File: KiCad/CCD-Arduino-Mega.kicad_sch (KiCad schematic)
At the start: 36 parts, among them J1 CCD+, J10 +5V, J11 PWM, J12 PWM, J13 COMMUNICATION, J2 CCD-, J3 Ground, J4 CCD-BUS, J5 Button, J6 POWER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

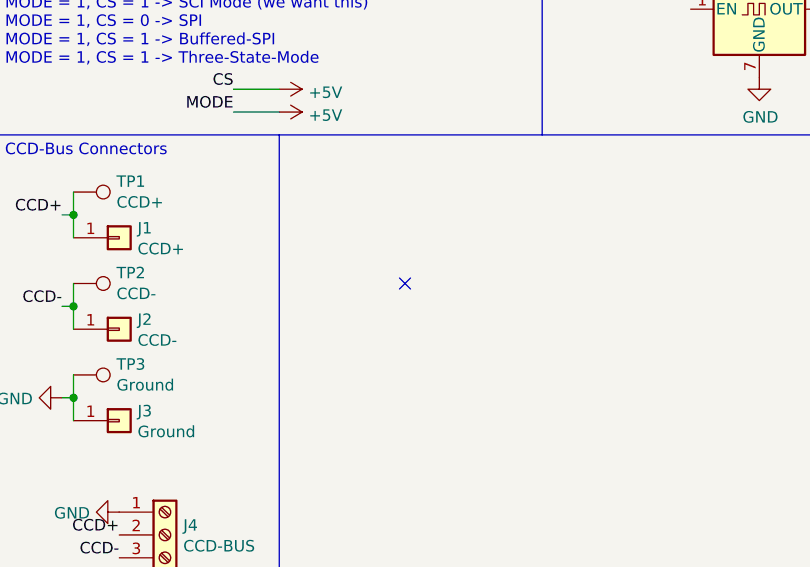
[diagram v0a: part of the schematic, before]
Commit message: implement ZIF-Socket
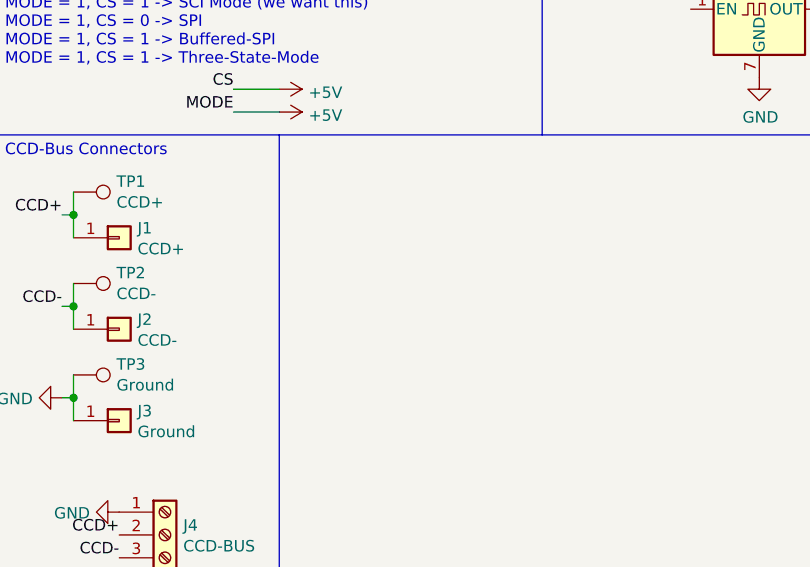
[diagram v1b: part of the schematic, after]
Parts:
- U1: footprint Package_DIP:DIP-14_W7.62mm -> Socket:DIP_Socket-14_W4.3_W5.08_W7.62_W10.16_W10.9_3M_214-3339-00-0602J
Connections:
- no-connect marks 6 -> 5
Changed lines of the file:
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@@
   (no_connect (at 76.2 49.53))
   (no_connect (at 76.2 22.86))
-  (no_connect (at 58.42 137.16))
   (polyline (pts (xy 12.7 170.18) (xy 44.45 170.18))
     (stroke (width 0) (type default) (color 0 0 0 0))
@@
     (property "Reference" "U1" (id 0) (at 41.91 18.6182 0))
     (property "Value" "Conn_02x07_Counter_Clockwise" (id 1) (at 41.91 20.9296 0))
-    (property "Footprint" "Package_DIP:DIP-14_W7.62mm" (id 2) (at 40.64 31.75 0)
+    (property "Footprint" "Socket:DIP_Socket-14_W4.3_W5.08_W7.62_W10.16_W10.9_3M_214-3339-00-0602J" (id 2) (at 40.64 31.75 0)
       (effects (font (size 1.27 1.27)) hide)
     )
@@
     )
     (path "/23352efa-710c-4ca4-98a5-fd92267e586c"
-      (reference "U1") (unit 1) (value "Conn_02x07_Counter_Clockwise") (footprint "Package_DIP:DIP-14_W7.62mm")
+      (reference "U1") (unit 1) (value "Conn_02x07_Counter_Clockwise") (footprint "Socket:DIP_Socket-14_W4.3_W5.08_W7.62_W10.16_W10.9_3M_214-3339-00-0602J")
     )
     (path "/99ad6875-75cb-427f-92c4-5fd2633b46f0"

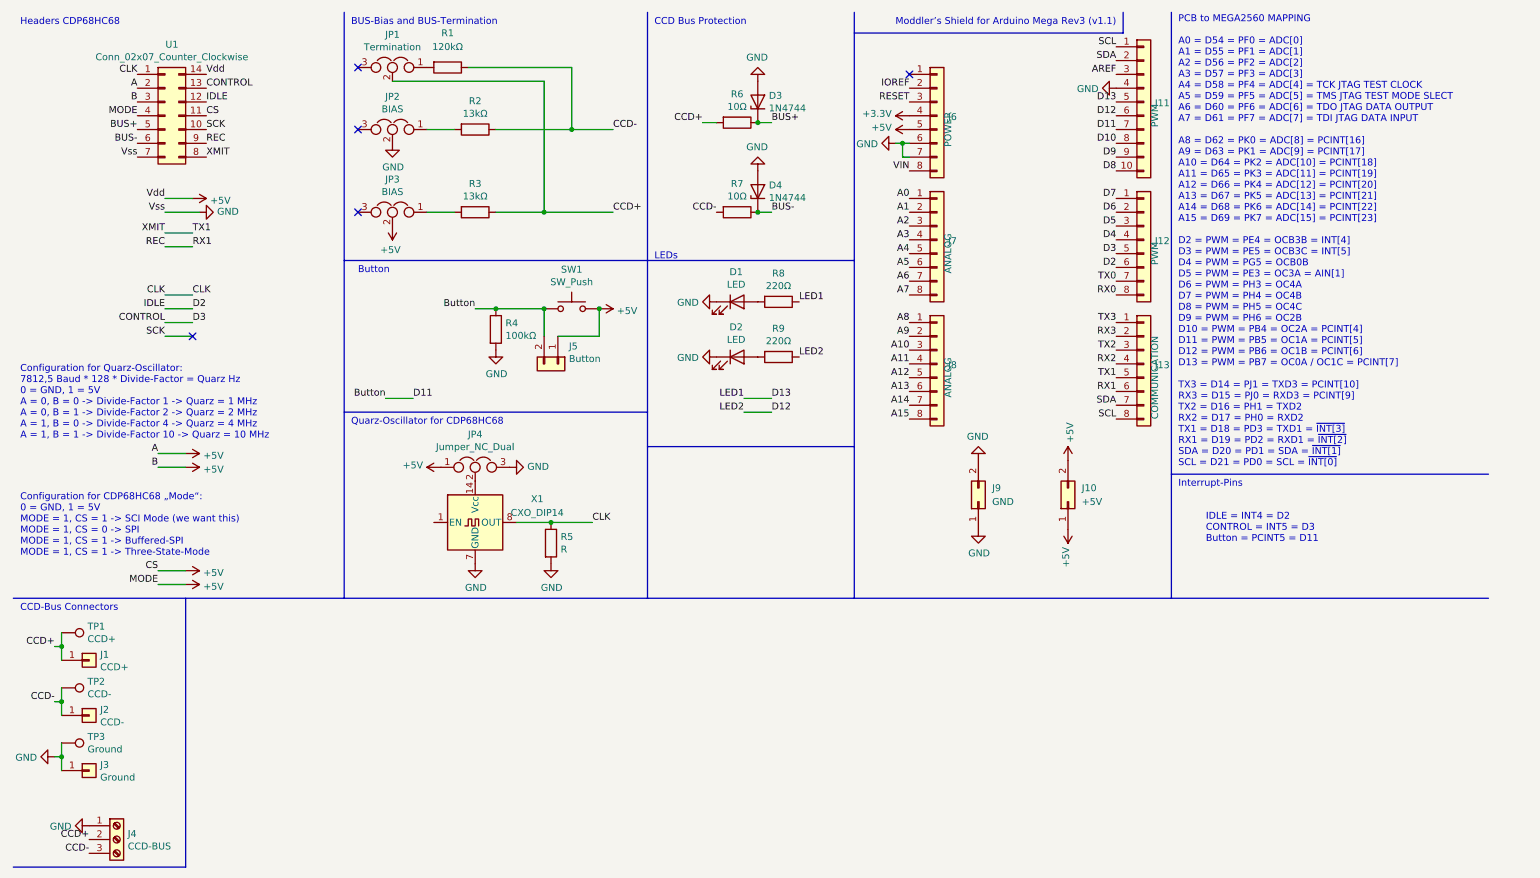
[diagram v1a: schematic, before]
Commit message: remove LED, connect CLK; Revision 1.0
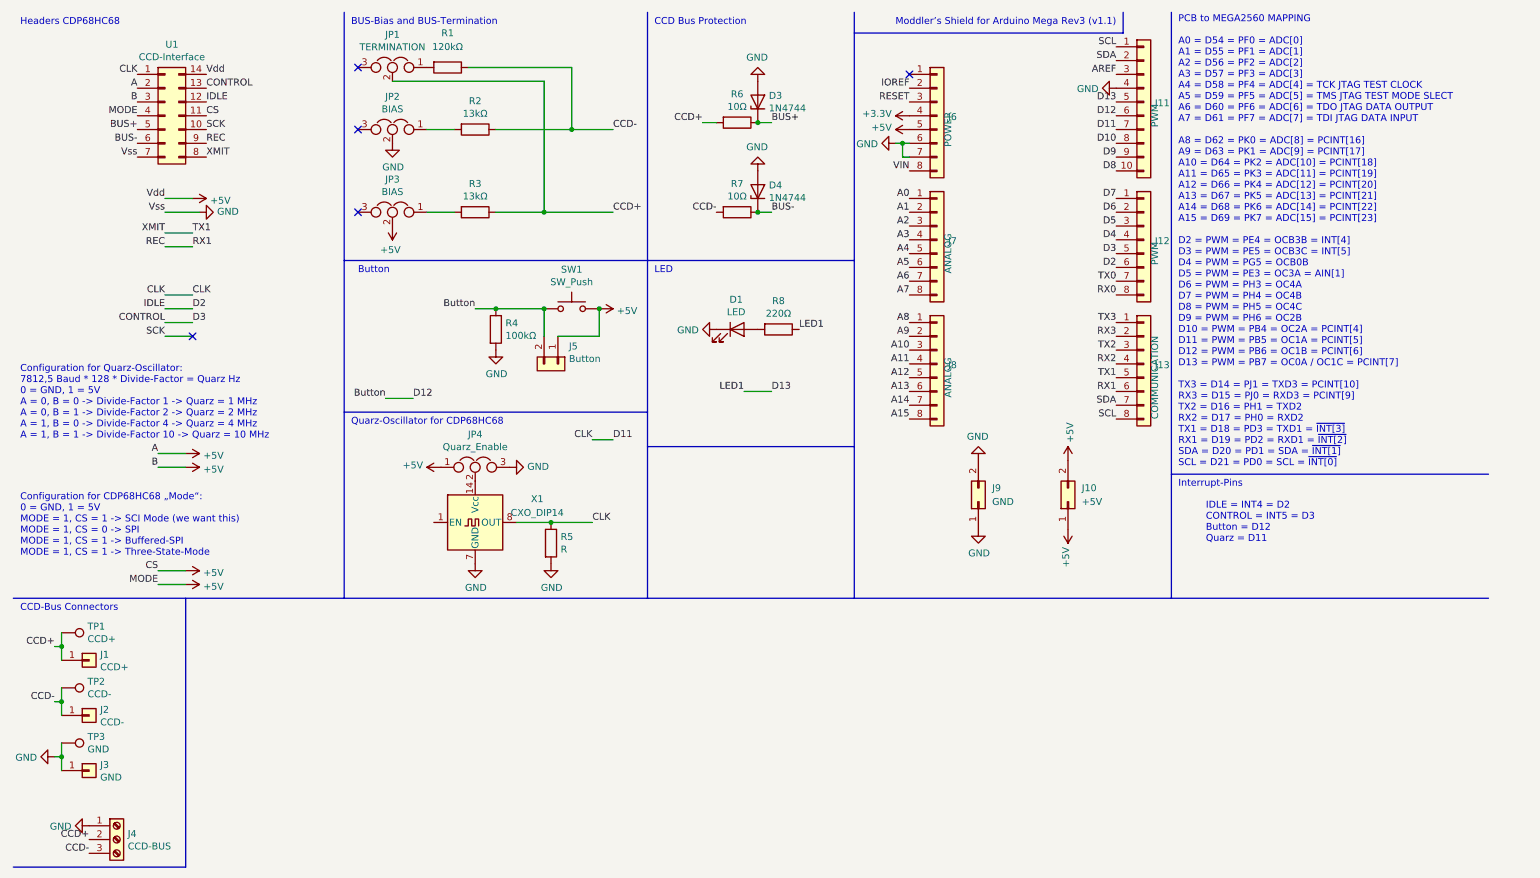
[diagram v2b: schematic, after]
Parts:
- removed D2: LED, LED_THT:LED_D5.0mm, symbol Device:LED
- removed R9: 220Ω, Resistor_THT:R_Axial_DIN0207_L6.3mm_D2.5mm_P7.62mm_Horizontal, symbol Device:R
- J3, TP3: value Ground -> GND
- JP1: value Termination -> TERMINATION
- JP4: value Jumper_NC_Dual -> Quarz_Enable
- U1: value Conn_02x07_Counter_Clockwise -> CCD-Interface
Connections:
- net D12 is gone; now on net Button: J11.6 (Pin_6)
- net Button: no longer J11.7 (Pin_7)
- net CLK: now also J11.7 (Pin_7)
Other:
- note added: "IDLE = INT4 = D2 CONTROL = INT5 = D3 Button = D12 Quarz = D11"
- note added: "LED"
- note removed: "IDLE = INT4 = D2 CONTROL = INT5 = D3 Button = PCINT5 = D11"
- note removed: "LEDs"
- company: (none) -> Moddler
- title: (none) -> CCD-Arduino-Mega
- moved on the sheet: D1, R8

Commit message: Update CCD-Arduino-Mega.kicad_sch
correct CCD-bus termination resistor value
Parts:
- R1: value 120kΩ -> 120Ω
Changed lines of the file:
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@@
     (in_bom yes) (on_board yes) (fields_autoplaced)
     (property "Reference" "R1" (id 0) (at 92.71 16.51 90))
-    (property "Value" "120kΩ" (id 1) (at 92.71 19.05 90))
+    (property "Value" "120Ω" (id 1) (at 92.71 19.05 90))
     (property "Footprint" "Resistor_THT:R_Axial_DIN0207_L6.3mm_D2.5mm_P7.62mm_Horizontal" (id 2) (at 92.71 21.082 90)
       (effects (font (size 1.27 1.27)) hide)
@@
     )
     (path "/000cc06b-ddc1-4252-a8ba-1b095fa8262f"
-      (reference "R1") (unit 1) (value "120kΩ") (footprint "Resistor_THT:R_Axial_DIN0207_L6.3mm_D2.5mm_P7.62mm_Horizontal")
+      (reference "R1") (unit 1) (value "120Ω") (footprint "Resistor_THT:R_Axial_DIN0207_L6.3mm_D2.5mm_P7.62mm_Horizontal")
     )
     (path "/107dc1df-ec8e-4ef0-9b6b-e3c5ef1e2e97"
